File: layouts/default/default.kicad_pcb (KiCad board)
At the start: 2 copper layers, 19 parts

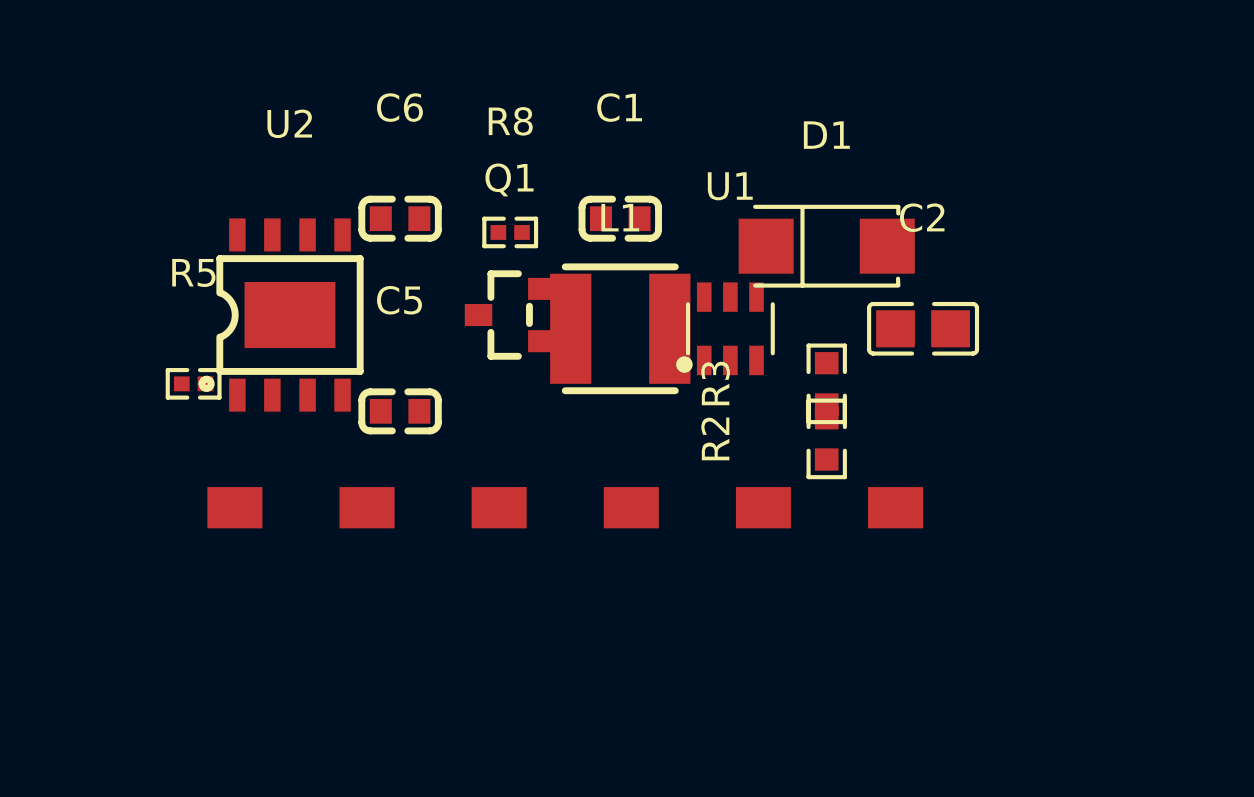
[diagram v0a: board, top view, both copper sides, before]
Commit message: Layout v2: proper spacing, 38x24mm board, GND pour, no overlaps
- Components spaced by actual footprint size
- 3 zones: charger (left) | MOSFET (center) | boost (right)
- Row 1 (y=87): ICs, inductor, diode
- Row 2 (y=95): small passives
- Row 3 (y=101.5): 6 solder pads, 6mm apart
- GND copper pour on B.Cu
- Clean silkscreen labels
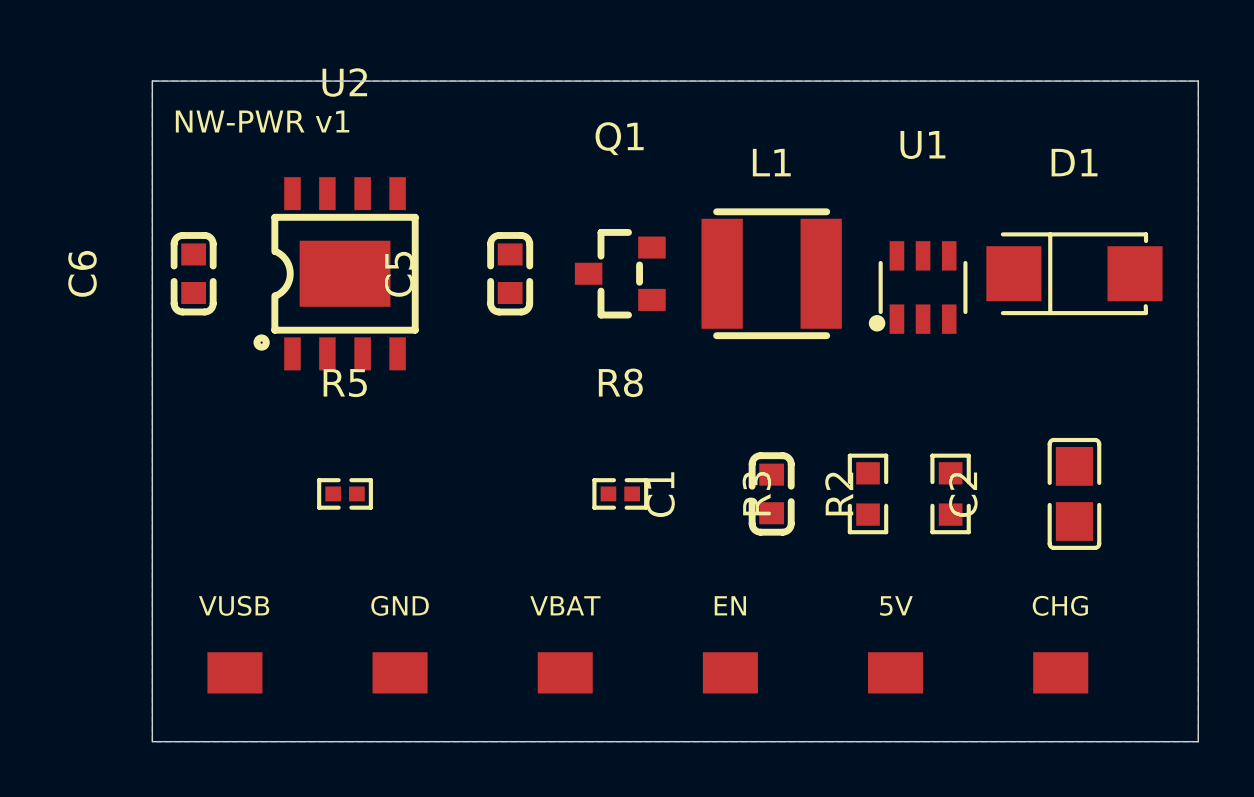
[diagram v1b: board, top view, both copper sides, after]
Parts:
- moved C1 11.4 mm to (122.5, 95.0), turned to 90 degrees
- moved R8 10.3 mm to (117.0, 95.0)
- moved D1 9.06 mm to (133.5, 87.0)
- moved J1 8.49 mm to (133.0, 101.5)
- moved C2 8.14 mm to (133.5, 95.0), turned to 90 degrees
- moved C6 7.76 mm to (101.5, 87.0), turned to 90 degrees
- moved J4 7.68 mm to (127.0, 101.5)
- moved U1 7.16 mm to (128.0, 87.5)
- moved J3 7.00 mm to (121.0, 101.5)
- moved R5 6.80 mm to (107.0, 95.0)
- moved J5 6.46 mm to (115.0, 101.5)
- moved C5 6.40 mm to (113.0, 87.0), turned to 90 degrees
- moved J2 6.12 mm to (109.0, 101.5)
- moved J6 6.00 mm to (103.0, 101.5)
- moved L1 5.85 mm to (122.5, 87.0)
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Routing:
- added copper zone on B.Cu, net lv
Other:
- board outline added: 38 x 24 mm
- board text added: "5V"
- board text added: "CHG"
- board text added: "EN"
- board text added: "GND"
- board text added: "NW-PWR v1"
- board text added: "VBAT"
- board text added: "VUSB"
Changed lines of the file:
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@@
 	(footprint "TOPPOWER_TP4056_42_ESOP8:ESOP-8_L4.9-W3.9-P1.27-LS6.0-BL-EP"
 		(layer "F.Cu")
-		(at 105 88.5)
+		(at 107 87)
 		(property "Reference" "U2"
 			(at 0 -6.91)
@@
 	(footprint "SX_SX1308:SOT-23-6_L2.9-W1.6-P0.95-LS2.8-BL"
 		(layer "F.Cu")
-		(at 121 89)
+		(at 128 87.5)
 		(property "Reference" "U1"
 			(at 0 -5.15)
@@
 	(footprint "Samsung_Electro_Mechanics_CL10A475KO8NNNC:C0603"
 		(layer "F.Cu")
-		(at 109 85)
+		(at 101.5 87 90)
 		(property "Reference" "C6"
-			(at 0 -4)
+			(at 0 -4 90)
 			(layer "F.SilkS")
 			(effects
@@
 		)
 		(property "Value" "0F"
-			(at 0 4)
+			(at 0 4 90)
 			(layer "F.Fab")
 			(effects
@@
 		)
 		(fp_text user "%R"
-			(at 0 0)
+			(at 0 0 90)
 			(layer "F.Fab")
 			(effects
@@
 		)
 		(pad "2" smd rect
-			(at 0.7 0 0)
+			(at 0.7 0 90)
 			(size 0.8 0.9)
 			(layers "F.Cu" "F.Paste" "F.Mask")
@@
 		)
 		(pad "1" smd rect
-			(at -0.7 0 0)
+			(at -0.7 0 90)
 			(size 0.8 0.9)
 			(layers "F.Cu" "F.Paste" "F.Mask")
@@
 	(footprint "UNI_ROYAL_0603WAF2203T5E:R0603"
 		(layer "F.Cu")
-		(at 124.5 91 90)
+		(at 126 95 90)
 		(property "Reference" "R3"
 			(at 0 -4 90)
@@
 	(footprint "Samsung_Electro_Mechanics_CL10A475KO8NNNC:C0603"
 		(layer "F.Cu")
-		(at 109 92)
+		(at 113 87 90)
 		(property "Reference" "C5"
-			(at 0 -4)
+			(at 0 -4 90)
 			(layer "F.SilkS")
 			(effects
@@
 		)
 		(property "Value" "0F"
-			(at 0 4)
+			(at 0 4 90)
 			(layer "F.Fab")
 			(effects
@@
 		)
 		(fp_text user "%R"
-			(at 0 0)
+			(at 0 0 90)
 			(layer "F.Fab")
 			(effects
@@
 		)
 		(pad "2" smd rect
-			(at 0.7 0 0)
+			(at 0.7 0 90)
 			(size 0.8 0.9)
 			(layers "F.Cu" "F.Paste" "F.Mask")
@@
 		)
 		(pad "1" smd rect
-			(at -0.7 0 0)
+			(at -0.7 0 90)
 			(size 0.8 0.9)
 			(layers "F.Cu" "F.Paste" "F.Mask")
@@
 	(footprint "SXN_SMNR4020_22UH:IND-SMD_L4.0-W4.0_LQH44PN2R2MP0L"
 		(layer "F.Cu")
-		(at 117 89)
+		(at 122.5 87)
 		(property "Reference" "L1"
 			(at 0 -4)
@@
 	(footprint "UNI_ROYAL_0402WGF2001TCE:R0402"
 		(layer "F.Cu")
-		(at 101.5 91)
+		(at 107 95)
 		(property "Reference" "R5"
 			(at 0 -4)
@@
 	(footprint "UNI_ROYAL_0603WAF3002T5E:R0603"
 		(layer "F.Cu")
-		(at 124.5 93 90)
+		(at 129 95 90)
 		(property "Reference" "R2"
 			(at 0 -4 90)
@@
 	(footprint "Alpha___Omega_Semicon_AO3401A:SOT-23_L2.9-W1.3-P1.90-LS2.4-BR"
 		(layer "F.Cu")
-		(at 113 88.5)
+		(at 117 87)
 		(property "Reference" "Q1"
 			(at 0 -4.95)
@@
 	(footprint "UNI_ROYAL_0402WGF1003TCE:R0402"
 		(layer "F.Cu")
-		(at 113 85.5)
+		(at 117 95)
 		(property "Reference" "R8"
 			(at 0 -4)
@@
 	(footprint "MDD_Microdiode_Electronics_SS34:SMA_L4.3-W2.6-LS5.2-RD"
 		(layer "F.Cu")
-		(at 124.5 86)
+		(at 133.5 87)
 		(property "Reference" "D1"
 			(at 0 -4)
@@
 	(footprint "Samsung_Electro_Mechanics_CL21A226MAQNNNE:C0805"
 		(layer "F.Cu")
-		(at 128 89)
+		(at 133.5 95 90)
 		(property "Reference" "C2"
-			(at 0 -4)
+			(at 0 -4 90)
 			(layer "F.SilkS")
 			(effects
@@
 		)
 		(property "Value" "0F"
-			(at 0 4)
+			(at 0 4 90)
 			(layer "F.Fab")
 			(effects
@@
 		)
 		(fp_text user "%R"
-			(at 0 0)
+			(at 0 0 90)
 			(layer "F.Fab")
 			(effects
@@
 		)
 		(pad "2" smd rect
-			(at 1 0 0)
+			(at 1 0 90)
 			(size 1.41 1.35)
 			(layers "F.Cu" "F.Paste" "F.Mask")
@@
 		)
 		(pad "1" smd rect
-			(at -1 0 0)
+			(at -1 0 90)
 			(size 1.41 1.35)
 			(layers "F.Cu" "F.Paste" "F.Mask")
@@
 	(footprint "Samsung_Electro_Mechanics_CL10A106KP8NNNC:C0603"
 		(layer "F.Cu")
-		(at 117 85)
+		(at 122.5 95 90)
 		(property "Reference" "C1"
-			(at 0 -4)
+			(at 0 -4 90)
 			(layer "F.SilkS")
 			(effects
@@
 		)
 		(property "Value" "0F"
-			(at 0 4)
+			(at 0 4 90)
 			(layer "F.Fab")
 			(effects
@@
 		)
 		(fp_text user "%R"
-			(at 0 0)
+			(at 0 0 90)
 			(layer "F.Fab")
 			(effects
@@
 		)
 		(pad "2" smd rect
-			(at 0.7 0 0)
+			(at 0.7 0 90)
 			(size 0.8 0.9)
 			(layers "F.Cu" "F.Paste" "F.Mask")
@@
 		)
 		(pad "1" smd rect
-			(at -0.7 0 0)
+			(at -0.7 0 90)
 			(size 0.8 0.9)
 			(layers "F.Cu" "F.Paste" "F.Mask")
@@
 	(footprint "SolderPad:SolderPad"
 		(layer "F.Cu")
-		(at 103 95.5)
+		(at 103 101.5)
 		(property "LCSC" "NA"
 			(at 0 0 0)
@@
 	(footprint "SolderPad:SolderPad"
 		(layer "F.Cu")
-		(at 107.8 95.5)
+		(at 109 101.5)
 		(property "LCSC" "NA"
 			(at 0 0 0)
@@
 	(footprint "SolderPad:SolderPad"
 		(layer "F.Cu")
-		(at 112.6 95.5)
+		(at 115 101.5)
 		(property "LCSC" "NA"
 			(at 0 0 0)
@@
 	(footprint "SolderPad:SolderPad"
 		(layer "F.Cu")
-		(at 122.2 95.5)
+		(at 127 101.5)
 		(property "LCSC" "NA"
 			(at 0 0 0)
@@
 	(footprint "SolderPad:SolderPad"
 		(layer "F.Cu")
-		(at 117.4 95.5)
+		(at 121 101.5)
 		(property "LCSC" "NA"
 			(at 0 0 0)
@@
 	(footprint "SolderPad:SolderPad"
 		(layer "F.Cu")
-		(at 127 95.5)
+		(at 133 101.5)
 		(property "LCSC" "NA"
 			(at 0 0 0)
@@
 		)
 	)
+	(gr_line
+		(start 100 80)
+		(end 138 80)
+		(stroke
+			(width 0.05)
+			(type default)
+		)
+		(layer "Edge.Cuts")
+	)
+	(gr_line
+		(start 138 80)
+		(end 138 104)
+		(stroke
+			(width 0.05)
+			(type default)
+		)
+		(layer "Edge.Cuts")
+	)
+	(gr_line
+		(start 138 104)
+		(end 100 104)
+		(stroke
+			(width 0.05)
+			(type default)
+		)
+		(layer "Edge.Cuts")
+	)
+	(gr_line
+		(start 100 104)
+		(end 100 80)
+		(stroke
+			(width 0.05)
+			(type default)
+		)
+		(layer "Edge.Cuts")
+	)
+	(gr_text "VUSB"
+		(at 103 99.5)
+		(layer "F.SilkS")
+		(effects
+			(font
+				(size 0.7 0.7)
+				(thickness 0.12)
+			)
+			(justify bottom)
+		)
+	)
+	(gr_text "GND"
+		(at 109 99.5)
+		(layer "F.SilkS")
+		(effects
+			(font
+				(size 0.7 0.7)
+				(thickness 0.12)
+			)
+			(justify bottom)
+		)
+	)
+	(gr_text "VBAT"
+		(at 115 99.5)
+		(layer "F.SilkS")
+		(effects
+			(font
+				(size 0.7 0.7)
+				(thickness 0.12)
+			)
+			(justify bottom)
+		)
+	)
+	(gr_text "EN"
+		(at 121 99.5)
+		(layer "F.SilkS")
+		(effects
+			(font
+				(size 0.7 0.7)
+				(thickness 0.12)
+			)
+			(justify bottom)
+		)
+	)
+	(gr_text "5V"
+		(at 127 99.5)
+		(layer "F.SilkS")
+		(effects
+			(font
+				(size 0.7 0.7)
+				(thickness 0.12)
+			)
+			(justify bottom)
+		)
+	)
+	(gr_text "CHG"
+		(at 133 99.5)
+		(layer "F.SilkS")
+		(effects
+			(font
+				(size 0.7 0.7)
+				(thickness 0.12)
+			)
+			(justify bottom)
+		)
+	)
+	(gr_text "NW-PWR v1"
+		(at 104 81.5)
+		(layer "F.SilkS")
+		(effects
+			(font
+				(size 0.8 0.8)
+				(thickness 0.12)
+			)
+		)
+	)
+	(zone
+		(net 15)
+		(net_name "lv")
+		(layer "B.Cu")
+		(hatch edge 0.5)
+		(connect_pads
+			(clearance 0.3)
+		)
+		(min_thickness 0.2)
+		(filled_areas_thickness no)
+		(fill yes
+			(thermal_gap 0.3)
+			(thermal_bridge_width 0.3)
+		)
+		(polygon
+			(pts
+				(xy 100 80) (xy 138 80) (xy 138 104) (xy 100 104)
+			)
+		)
+	)

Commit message: Layout v3: rounded corners, all components horizontal, proper spacing
- 1mm rounded corners on board outline
- All passives horizontal (no rotation surprises)
- C6 and C5 above U2 (not overlapping)
- R5 moved to row 2 with space
- R2/R3 feedback divider 4mm apart (no overlap)
- C1/C2 properly spaced in boost row 2
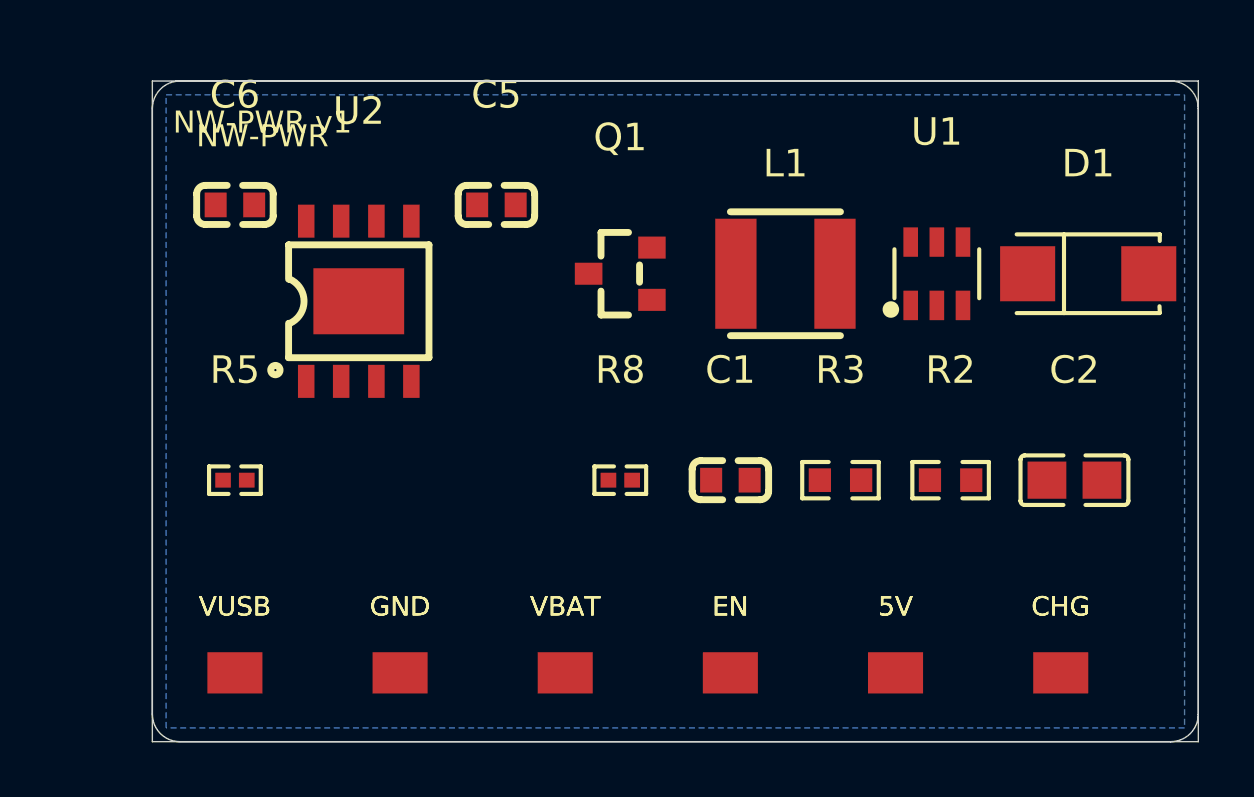
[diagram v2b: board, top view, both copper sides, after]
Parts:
- moved R5 4.03 mm to (103.0, 94.5)
- moved C6 2.92 mm to (103.0, 84.5), turned to 0 degrees
- moved C5 2.55 mm to (112.5, 84.5), turned to 0 degrees
- moved C1 1.58 mm to (121.0, 94.5), turned to 0 degrees
- moved R3 1.12 mm to (125.0, 94.5), turned to 0 degrees
- moved U2 1.12 mm to (107.5, 88.0)
- moved U1 0.71 mm to (128.5, 87.0)
- moved C2 0.50 mm to (133.5, 94.5), turned to 0 degrees
- moved D1 0.50 mm to (134.0, 87.0)
- moved L1 0.50 mm to (123.0, 87.0)
- moved R2 0.50 mm to (129.0, 94.5), turned to 0 degrees
- moved R8 0.50 mm to (117.0, 94.5)
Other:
- outline, holes or cut-outs redrawn
- board text added: "NW-PWR"
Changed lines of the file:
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@@
 	(footprint "TOPPOWER_TP4056_42_ESOP8:ESOP-8_L4.9-W3.9-P1.27-LS6.0-BL-EP"
 		(layer "F.Cu")
-		(at 107 87)
+		(at 107.5 88)
 		(property "Reference" "U2"
 			(at 0 -6.91)
@@
 	(footprint "SX_SX1308:SOT-23-6_L2.9-W1.6-P0.95-LS2.8-BL"
 		(layer "F.Cu")
-		(at 128 87.5)
+		(at 128.5 87)
 		(property "Reference" "U1"
 			(at 0 -5.15)
@@
 	(footprint "Samsung_Electro_Mechanics_CL10A475KO8NNNC:C0603"
 		(layer "F.Cu")
-		(at 101.5 87 90)
+		(at 103 84.5)
 		(property "Reference" "C6"
-			(at 0 -4 90)
+			(at 0 -4)
 			(layer "F.SilkS")
 			(effects
@@
 		)
 		(property "Value" "0F"
-			(at 0 4 90)
+			(at 0 4)
 			(layer "F.Fab")
 			(effects
@@
 		)
 		(fp_text user "%R"
-			(at 0 0 90)
+			(at 0 0)
 			(layer "F.Fab")
 			(effects
@@
 		)
 		(pad "2" smd rect
-			(at 0.7 0 90)
+			(at 0.7 0 0)
 			(size 0.8 0.9)
 			(layers "F.Cu" "F.Paste" "F.Mask")
@@
 		)
 		(pad "1" smd rect
-			(at -0.7 0 90)
+			(at -0.7 0 0)
 			(size 0.8 0.9)
 			(layers "F.Cu" "F.Paste" "F.Mask")
@@
 	(footprint "UNI_ROYAL_0603WAF2203T5E:R0603"
 		(layer "F.Cu")
-		(at 126 95 90)
+		(at 125 94.5)
 		(property "Reference" "R3"
-			(at 0 -4 90)
+			(at 0 -4)
 			(layer "F.SilkS")
 			(effects
@@
 		)
 		(property "Value" "220000Ω"
-			(at 0 4 90)
+			(at 0 4)
 			(layer "F.Fab")
 			(effects
@@
 		)
 		(fp_text user "%R"
-			(at 0 0 90)
+			(at 0 0)
 			(layer "F.Fab")
 			(effects
@@
 		)
 		(pad "2" smd rect
-			(at 0.75 0 90)
+			(at 0.75 0 0)
 			(size 0.81 0.86)
 			(layers "F.Cu" "F.Paste" "F.Mask")
@@
 		)
 		(pad "1" smd rect
-			(at -0.75 0 90)
+			(at -0.75 0 0)
 			(size 0.81 0.86)
 			(layers "F.Cu" "F.Paste" "F.Mask")
@@
 	(footprint "Samsung_Electro_Mechanics_CL10A475KO8NNNC:C0603"
 		(layer "F.Cu")
-		(at 113 87 90)
+		(at 112.5 84.5)
 		(property "Reference" "C5"
-			(at 0 -4 90)
+			(at 0 -4)
 			(layer "F.SilkS")
 			(effects
@@
 		)
 		(property "Value" "0F"
-			(at 0 4 90)
+			(at 0 4)
 			(layer "F.Fab")
 			(effects
@@
 		)
 		(fp_text user "%R"
-			(at 0 0 90)
+			(at 0 0)
 			(layer "F.Fab")
 			(effects
@@
 		)
 		(pad "2" smd rect
-			(at 0.7 0 90)
+			(at 0.7 0 0)
 			(size 0.8 0.9)
 			(layers "F.Cu" "F.Paste" "F.Mask")
@@
 		)
 		(pad "1" smd rect
-			(at -0.7 0 90)
+			(at -0.7 0 0)
 			(size 0.8 0.9)
 			(layers "F.Cu" "F.Paste" "F.Mask")
@@
 	(footprint "SXN_SMNR4020_22UH:IND-SMD_L4.0-W4.0_LQH44PN2R2MP0L"
 		(layer "F.Cu")
-		(at 122.5 87)
+		(at 123 87)
 		(property "Reference" "L1"
 			(at 0 -4)
@@
 	(footprint "UNI_ROYAL_0402WGF2001TCE:R0402"
 		(layer "F.Cu")
-		(at 107 95)
+		(at 103 94.5)
 		(property "Reference" "R5"
 			(at 0 -4)
@@
 	(footprint "UNI_ROYAL_0603WAF3002T5E:R0603"
 		(layer "F.Cu")
-		(at 129 95 90)
+		(at 129 94.5)
 		(property "Reference" "R2"
-			(at 0 -4 90)
+			(at 0 -4)
 			(layer "F.SilkS")
 			(effects
@@
 		)
 		(property "Value" "30000Ω"
-			(at 0 4 90)
+			(at 0 4)
 			(layer "F.Fab")
 			(effects
@@
 		)
 		(fp_text user "%R"
-			(at 0 0 90)
+			(at 0 0)
 			(layer "F.Fab")
 			(effects
@@
 		)
 		(pad "2" smd rect
-			(at 0.75 0 90)
+			(at 0.75 0 0)
 			(size 0.81 0.86)
 			(layers "F.Cu" "F.Paste" "F.Mask")
@@
 		)
 		(pad "1" smd rect
-			(at -0.75 0 90)
+			(at -0.75 0 0)
 			(size 0.81 0.86)
 			(layers "F.Cu" "F.Paste" "F.Mask")
@@
 	(footprint "UNI_ROYAL_0402WGF1003TCE:R0402"
 		(layer "F.Cu")
-		(at 117 95)
+		(at 117 94.5)
 		(property "Reference" "R8"
 			(at 0 -4)
@@
 	(footprint "MDD_Microdiode_Electronics_SS34:SMA_L4.3-W2.6-LS5.2-RD"
 		(layer "F.Cu")
-		(at 133.5 87)
+		(at 134 87)
 		(property "Reference" "D1"
 			(at 0 -4)
@@
 	(footprint "Samsung_Electro_Mechanics_CL21A226MAQNNNE:C0805"
 		(layer "F.Cu")
-		(at 133.5 95 90)
+		(at 133.5 94.5)
 		(property "Reference" "C2"
-			(at 0 -4 90)
+			(at 0 -4)
 			(layer "F.SilkS")
 			(effects
@@
 		)
 		(property "Value" "0F"
-			(at 0 4 90)
+			(at 0 4)
 			(layer "F.Fab")
 			(effects
@@
 		)
 		(fp_text user "%R"
-			(at 0 0 90)
+			(at 0 0)
 			(layer "F.Fab")
 			(effects
@@
 		)
 		(pad "2" smd rect
-			(at 1 0 90)
+			(at 1 0 0)
 			(size 1.41 1.35)
 			(layers "F.Cu" "F.Paste" "F.Mask")
@@
 		)
 		(pad "1" smd rect
-			(at -1 0 90)
+			(at -1 0 0)
 			(size 1.41 1.35)
 			(layers "F.Cu" "F.Paste" "F.Mask")
@@
 	(footprint "Samsung_Electro_Mechanics_CL10A106KP8NNNC:C0603"
 		(layer "F.Cu")
-		(at 122.5 95 90)
+		(at 121 94.5)
 		(property "Reference" "C1"
-			(at 0 -4 90)
+			(at 0 -4)
 			(layer "F.SilkS")
 			(effects
@@
 		)
 		(property "Value" "0F"
-			(at 0 4 90)
+			(at 0 4)
 			(layer "F.Fab")
 			(effects
@@
 		)
 		(fp_text user "%R"
-			(at 0 0 90)
+			(at 0 0)
 			(layer "F.Fab")
 			(effects
@@
 		)
 		(pad "2" smd rect
-			(at 0.7 0 90)
+			(at 0.7 0 0)
 			(size 0.8 0.9)
 			(layers "F.Cu" "F.Paste" "F.Mask")
@@
 		)
 		(pad "1" smd rect
-			(at -0.7 0 90)
+			(at -0.7 0 0)
 			(size 0.8 0.9)
 			(layers "F.Cu" "F.Paste" "F.Mask")
@@
 		(layer "Edge.Cuts")
 	)
+	(gr_line
+		(start 101 80)
+		(end 137 80)
+		(stroke
+			(width 0.05)
+			(type default)
+		)
+		(layer "Edge.Cuts")
+	)
+	(gr_line
+		(start 138 81)
+		(end 138 103)
+		(stroke
+			(width 0.05)
+			(type default)
+		)
+		(layer "Edge.Cuts")
+	)
+	(gr_line
+		(start 137 104)
+		(end 101 104)
+		(stroke
+			(width 0.05)
+			(type default)
+		)
+		(layer "Edge.Cuts")
+	)
+	(gr_line
+		(start 100 103)
+		(end 100 81)
+		(stroke
+			(width 0.05)
+			(type default)
+		)
+		(layer "Edge.Cuts")
+	)
+	(gr_arc
+		(start 137 80)
+		(mid 137.7071 80.2929)
+		(end 138 81)
+		(stroke
+			(width 0.05)
+			(type default)
+		)
+		(layer "Edge.Cuts")
+	)
+	(gr_arc
+		(start 138 103)
+		(mid 137.7071 103.7071)
+		(end 137 104)
+		(stroke
+			(width 0.05)
+			(type default)
+		)
+		(layer "Edge.Cuts")
+	)
+	(gr_arc
+		(start 101 104)
+		(mid 100.2929 103.7071)
+		(end 100 103)
+		(stroke
+			(width 0.05)
+			(type default)
+		)
+		(layer "Edge.Cuts")
+	)
+	(gr_arc
+		(start 100 81)
+		(mid 100.2929 80.2929)
+		(end 101 80)
+		(stroke
+			(width 0.05)
+			(type default)
+		)
+		(layer "Edge.Cuts")
+	)
 	(gr_text "VUSB"
 		(at 103 99.5)
@@
 		)
 	)
+	(gr_text "VUSB"
+		(at 103 99.5)
+		(layer "F.SilkS")
+		(effects
+			(font
+				(size 0.7 0.7)
+				(thickness 0.12)
+			)
+			(justify bottom)
+		)
+	)
+	(gr_text "GND"
+		(at 109 99.5)
+		(layer "F.SilkS")
+		(effects
+			(font
+				(size 0.7 0.7)
+				(thickness 0.12)
+			)
+			(justify bottom)
+		)
+	)
+	(gr_text "VBAT"
+		(at 115 99.5)
+		(layer "F.SilkS")
+		(effects
+			(font
+				(size 0.7 0.7)
+				(thickness 0.12)
+			)
+			(justify bottom)
+		)
+	)
+	(gr_text "EN"
+		(at 121 99.5)
+		(layer "F.SilkS")
+		(effects
+			(font
+				(size 0.7 0.7)
+				(thickness 0.12)
+			)
+			(justify bottom)
+		)
+	)
+	(gr_text "5V"
+		(at 127 99.5)
+		(layer "F.SilkS")
+		(effects
+			(font
+				(size 0.7 0.7)
+				(thickness 0.12)
+			)
+			(justify bottom)
+		)
+	)
+	(gr_text "CHG"
+		(at 133 99.5)
+		(layer "F.SilkS")
+		(effects
+			(font
+				(size 0.7 0.7)
+				(thickness 0.12)
+			)
+			(justify bottom)
+		)
+	)
+	(gr_text "NW-PWR"
+		(at 104 82)
+		(layer "F.SilkS")
+		(effects
+			(font
+				(size 0.8 0.8)
+				(thickness 0.12)
+			)
+		)
+	)
 	(zone
 		(net 15)
@@
 		(polygon
 			(pts
-				(xy 100 80) (xy 138 80) (xy 138 104) (xy 100 104)
+				(xy 100.5 80.5) (xy 137.5 80.5) (xy 137.5 103.5) (xy 100.5 103.5)
 			)
 		)
